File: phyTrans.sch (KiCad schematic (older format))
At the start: 8 parts

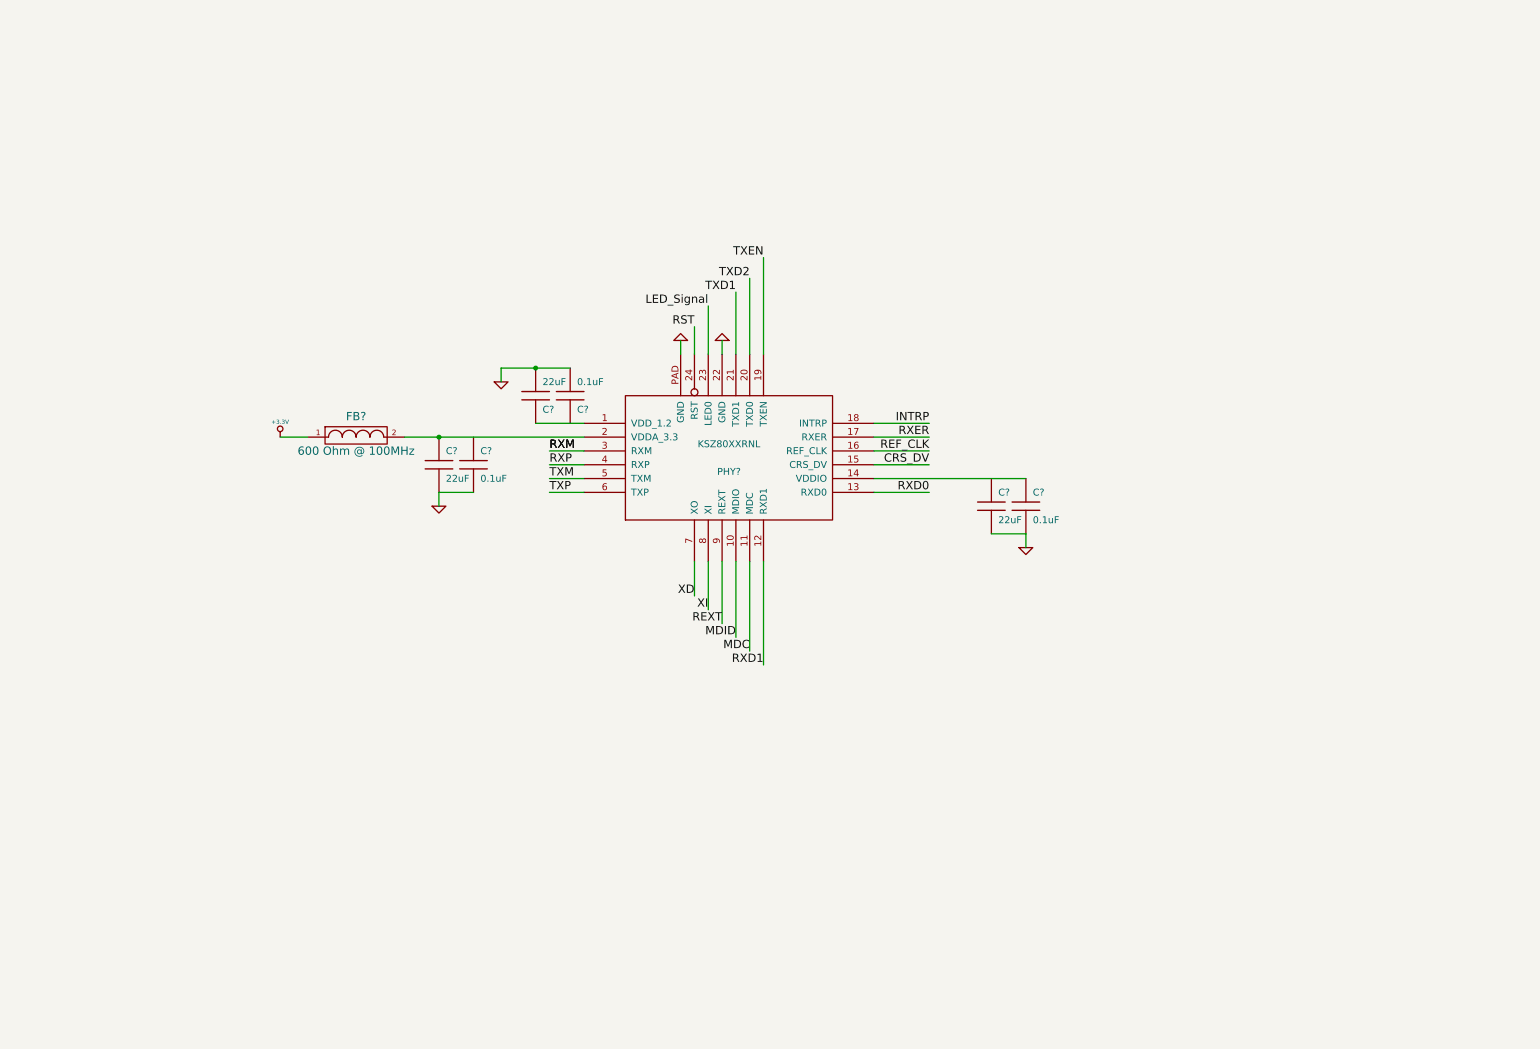
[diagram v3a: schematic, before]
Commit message: Made quite a few changes... The Eth Phy and RJ-45 connection should be close to finished. Figured out how to make the hierarchical sheets work.
Need to move the power schematic to a hierarchical sheet.
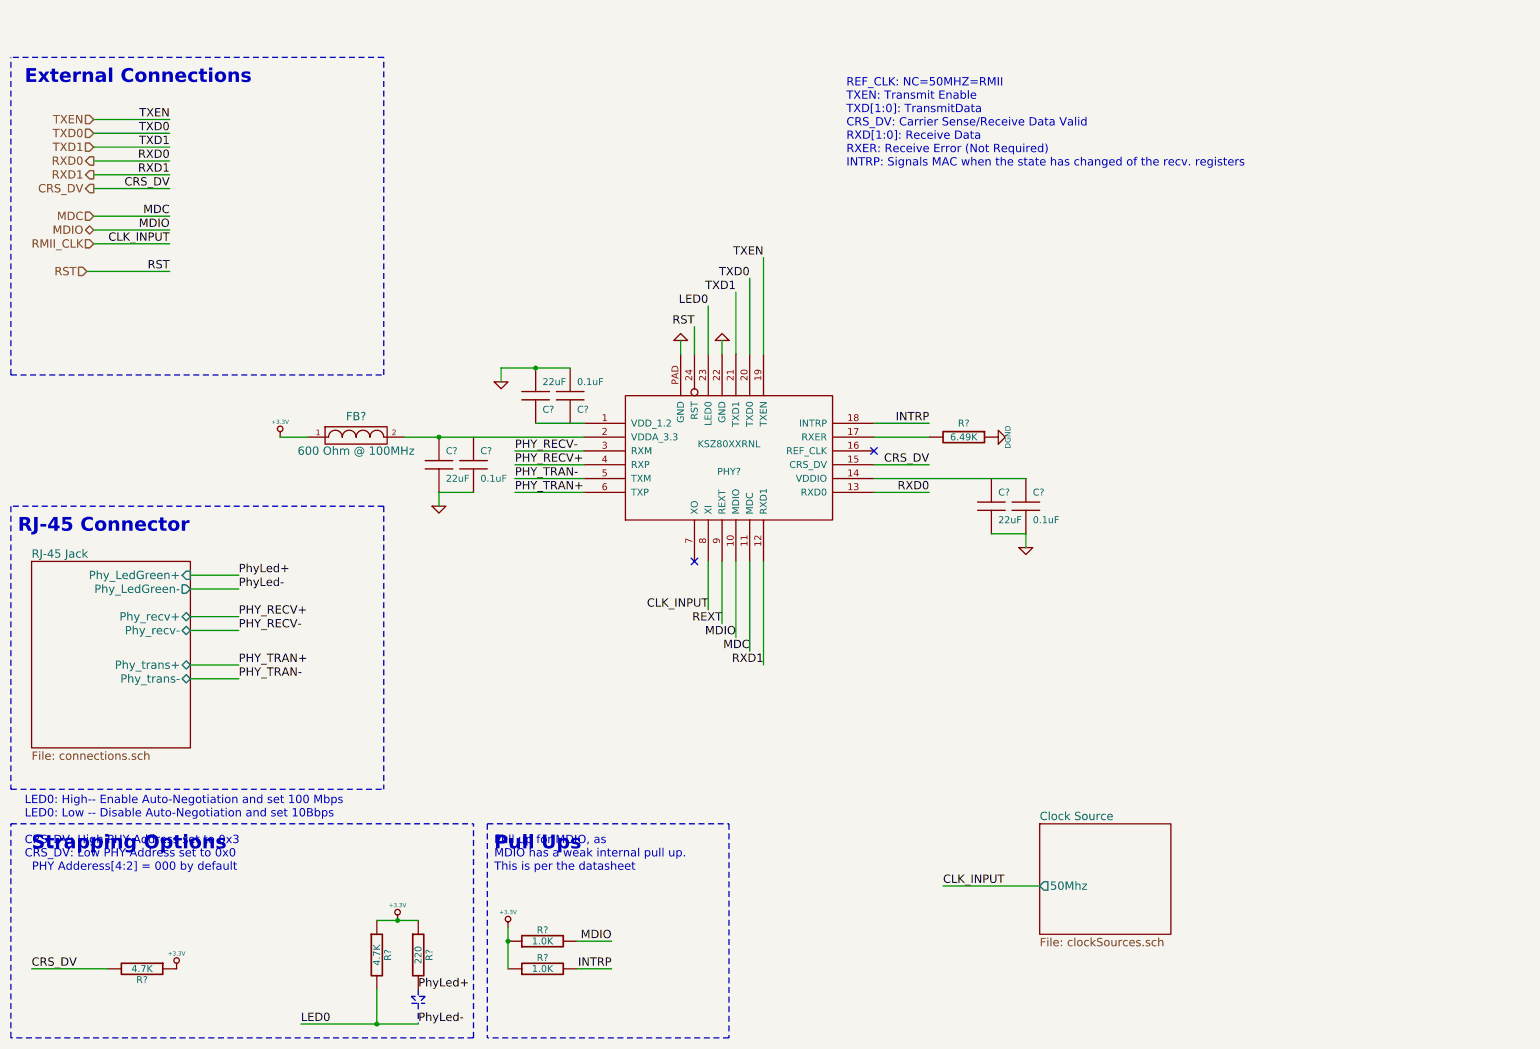
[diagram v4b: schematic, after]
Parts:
- added R?: 6.49K, symbol R
- added R? (x2): 1.0K, symbol R
- added R? (x2): 4.7K, symbol R
- added R?: 220, symbol R
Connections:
- net +3.3V: now also R?.1, R?.1, R?.1, R?.1, R?.1
- net CRS_DV: now also R?.2
- net INTRP: now also R?.2
- net LED_Signal renamed LED0
- net LED0: now also R?.2
- net MDID renamed MDIO
- net MDIO: now also R?.2
- net REF_CLK: no longer names the net of PHY?.16 (REF_CLK)
- net RXER: no longer names the net of PHY?.17 (RXER)
- net RXER: now also R?.2
- net RXM renamed PHY_RECV-
- net RXP renamed PHY_RECV+
- net TXD2 renamed TXD0
- net TXM renamed PHY_TRAN-
- net TXP renamed PHY_TRAN+
- net XD: no longer names the net of PHY?.7 (XO)
- net XI renamed RMII_CLK
- new net DGND: R?.1
- new net PhyLed+: R?.2
- no-connect marks 0 -> 2
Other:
- note added: "External Connections"
- note added: "LED0: High-- Enable Auto-Negotiation and set 100 Mbps\nLED0: Low -- Disable Auto-Negotiation and set 10Bbps\n\nCRS_DV: High PHY Address set to 0x3\nCRS_DV: Low PHY Address set to 0x0\n PHY Adderess[4:2] = 000 by default"
- note added: "Pull Ups"
- note added: "Pull up for MDIO, as \nMDIO has a weak internal pull up. \nThis is per the datasheet\n"
- note added: "REF_CLK: NC=50MHZ=RMII\nTXEN: Transmit Enable\nTXD[1:0]: TransmitData\nCRS_DV: Carrier Sense/Receive Data Valid\nRXD[1:0]: Receive Data\nRXER: Receive Error (Not Required)\nINTRP: Signals MAC when the state has changed of the recv. registers"
- note added: "RJ-45 Connector"
- note added: "Strapping Options"

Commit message: Made the Clock Source for the Phy. Removed the 50MHz OSC from the notes page.
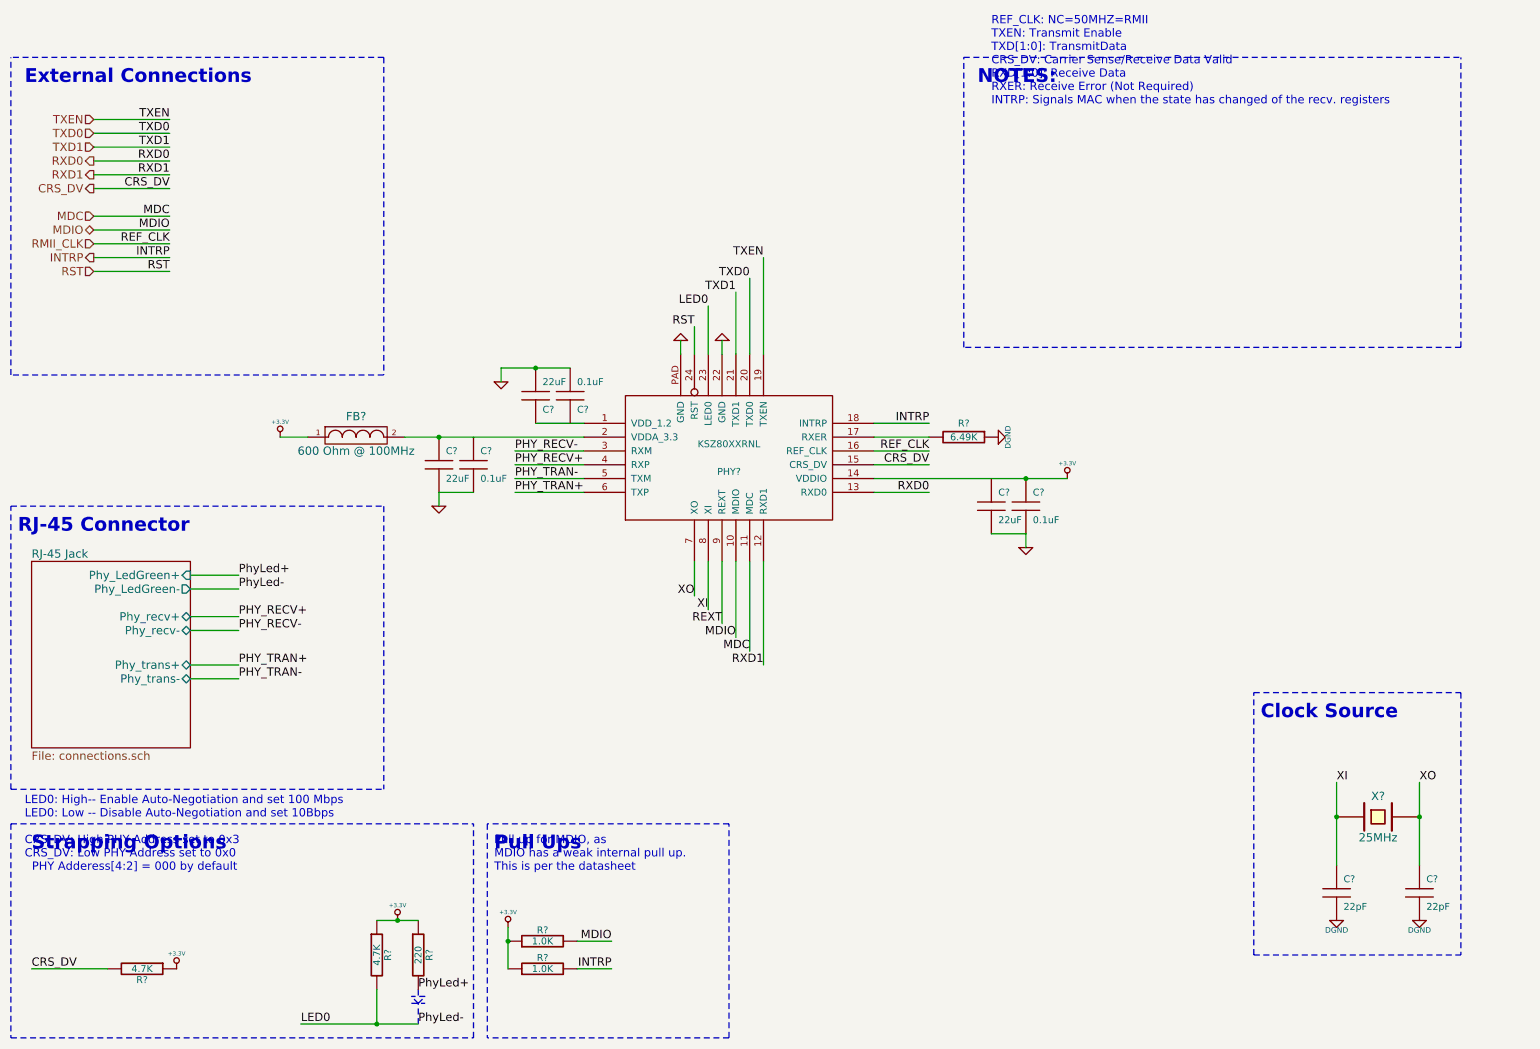
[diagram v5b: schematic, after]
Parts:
- added C? (x2): 22pF, symbol C
- added X?: 25MHz, symbol CRYSTAL
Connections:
- net +3.3V: now also C?.1, PHY?.14 (VDDIO)
- net DGND: now also C?.2, C?.2
- net RMII_CLK: now also PHY?.16 (REF_CLK); no longer PHY?.8 (XI)
- net XO: now reaches PHY?.7 (XO)
- net XO: now also C?.1, X?.2
- new net XI: C?.1, PHY?.8 (XI), X?.1
- no-connect marks 2 -> 0
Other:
- note added: "Clock Source"
- note added: "NOTES:"
